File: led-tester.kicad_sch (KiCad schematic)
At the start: 19 parts, among them M1 Arduino_Mini, U1 PCF8591

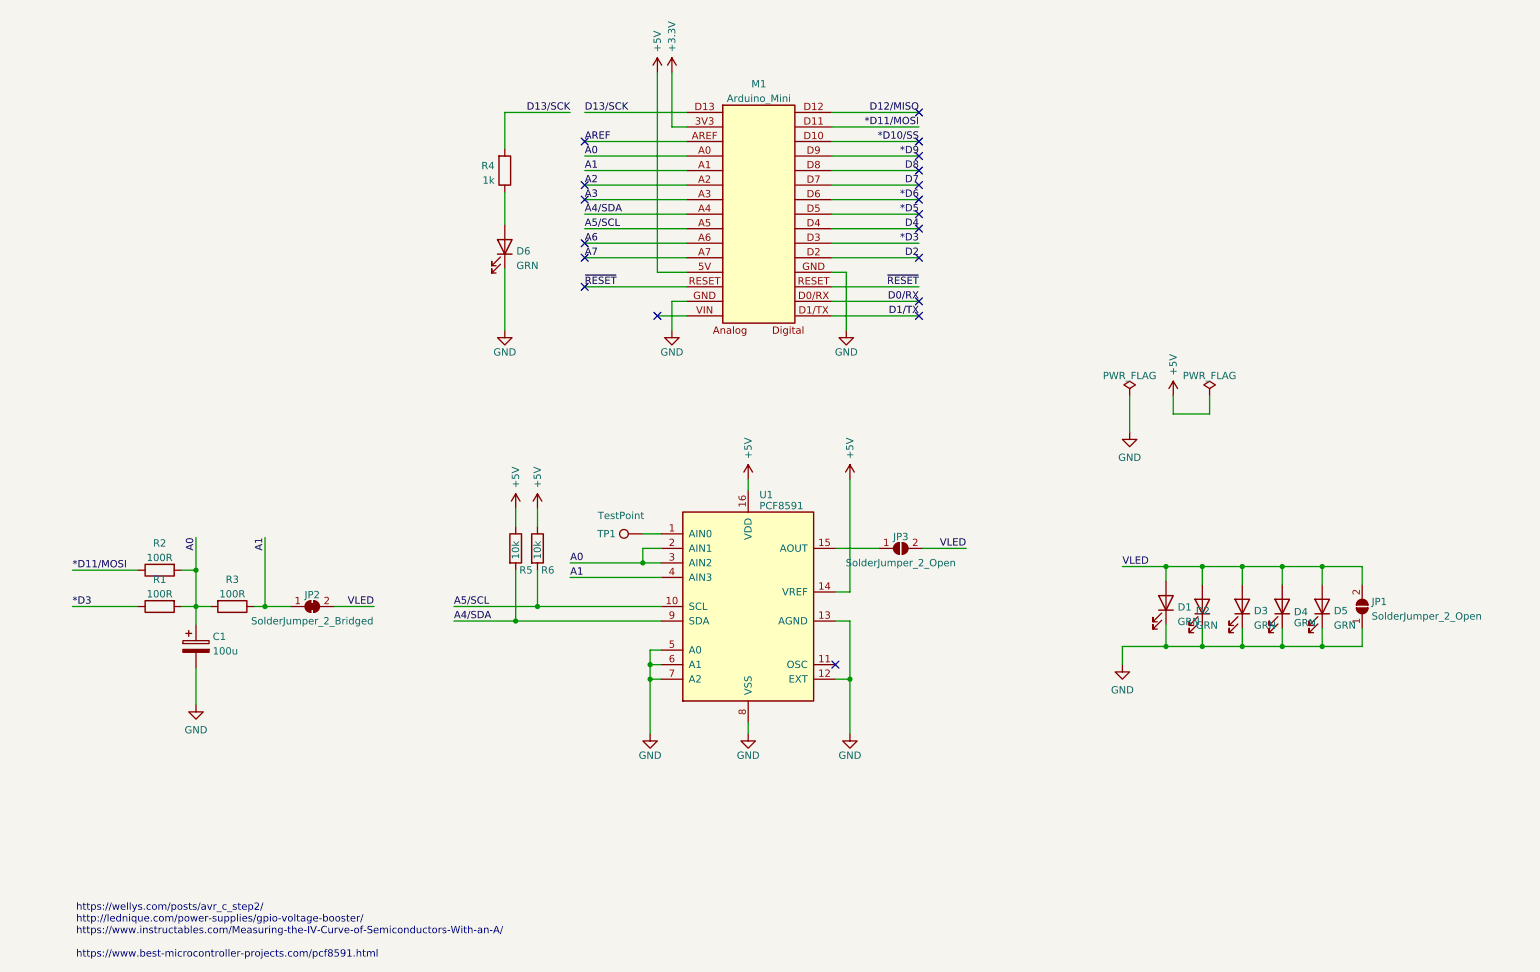
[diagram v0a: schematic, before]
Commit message: Added a current sense resistor, a decoupling cap, and rewired the PCF8591 analog inputs.
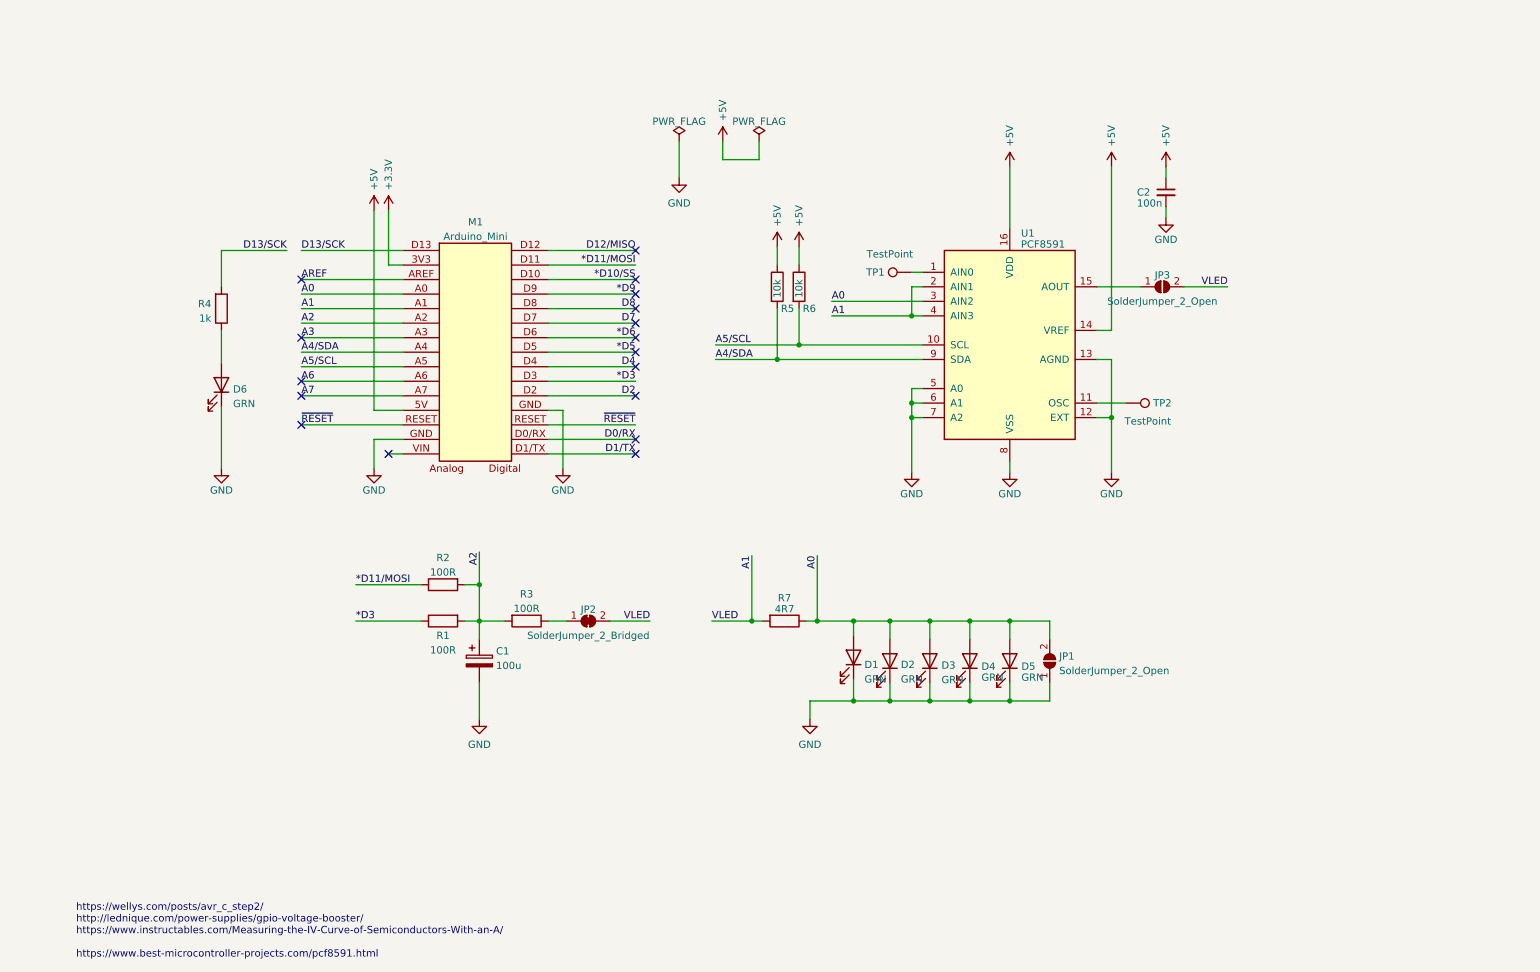
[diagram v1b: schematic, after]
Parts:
- added C2: 100n, Capacitor_SMD:C_0805_2012Metric_Pad1.18x1.45mm_HandSolder, symbol Device:C_Small
- added R7: 4R7, Resistor_SMD:R_0805_2012Metric_Pad1.20x1.40mm_HandSolder, symbol Device:R
- added TP2: TestPoint, TestPoint:TestPoint_Pad_1.5x1.5mm, symbol Connector:TestPoint
- renumbered D5 to D4, D4 to D5
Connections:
- net +5V: now also C2.1
- net A0: now also D1.2 (A), D2.2 (A), D3.2 (A), D4.2 (A), D5.2 (A), JP1.2 (B), R7.1; no longer C1.1, R1.2, R2.2, R3.2, U1.2 (AIN1)
- net A1: now also JP2.2 (B), JP3.2 (B), U1.2 (AIN1), R7.2; no longer JP2.1 (A), R3.1
- net A2: now also C1.1, R1.2, R2.2, R3.2
- net GND: now also C2.2
- net at U1.11 (OSC): now also TP2.1
- removed net VLED: D1.2 (A), D2.2 (A), D3.2 (A), D4.2 (A), D5.2 (A), JP1.2 (B), JP2.2 (B), JP3.2 (B)
- new net: JP2.1 (A), R3.1
- no-connect marks 19 -> 17
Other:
- moved on the sheet: C1, D1, D2, D3, D4, D5, D6, JP1, JP2, JP3, M1, R1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

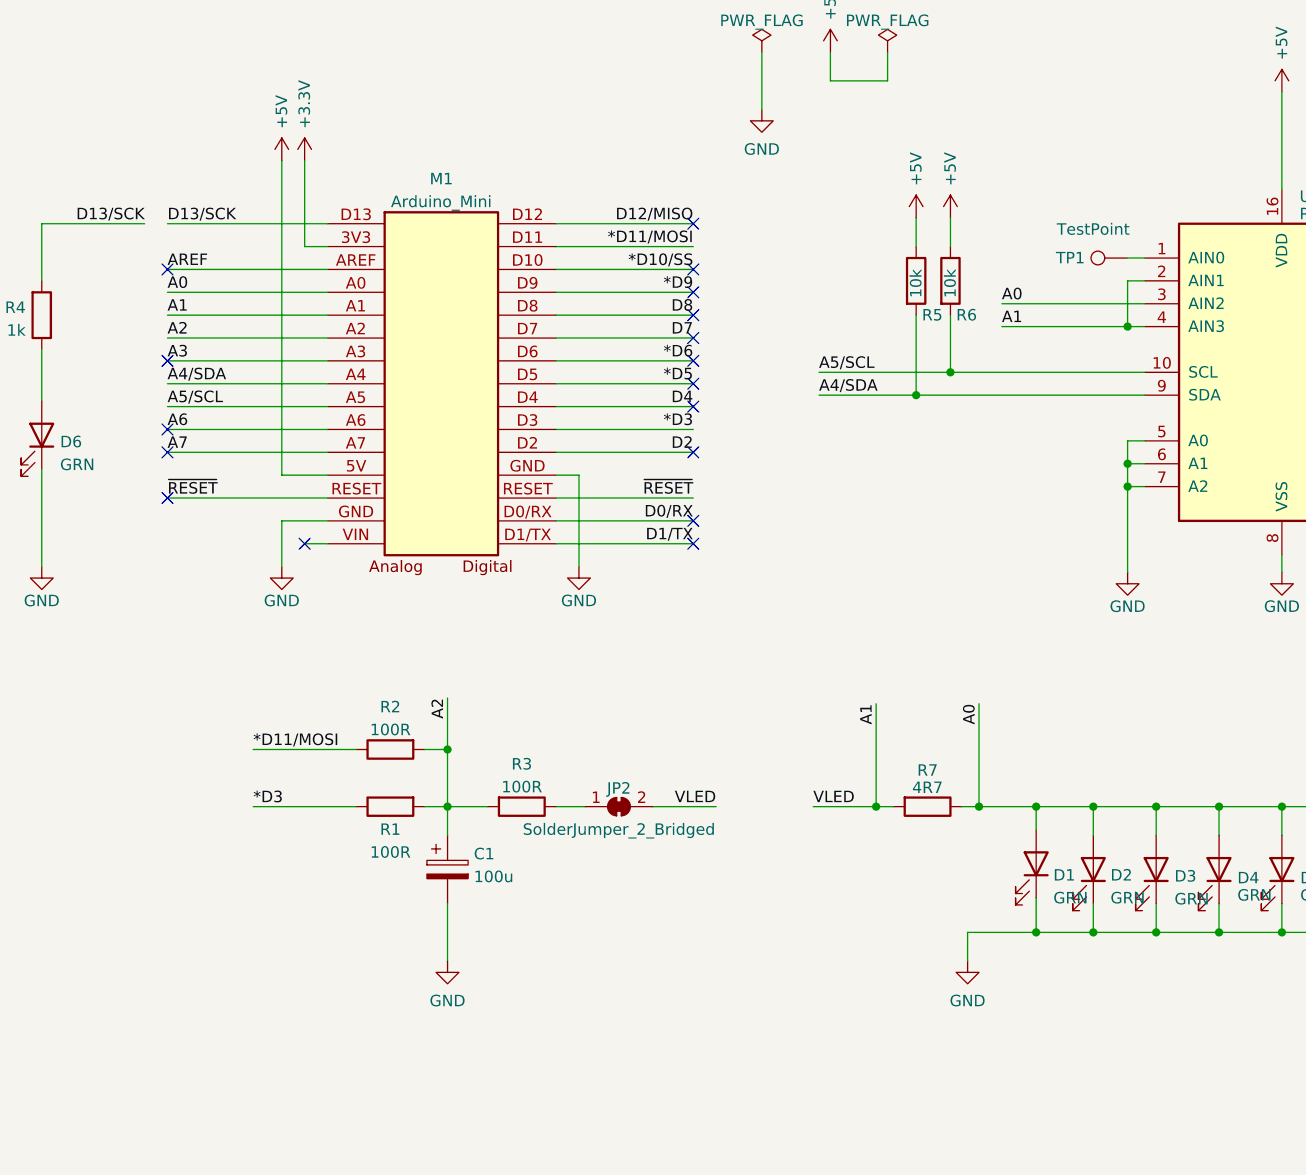
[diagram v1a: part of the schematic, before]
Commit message: Added a sense resistor between the LED under test, and GND.
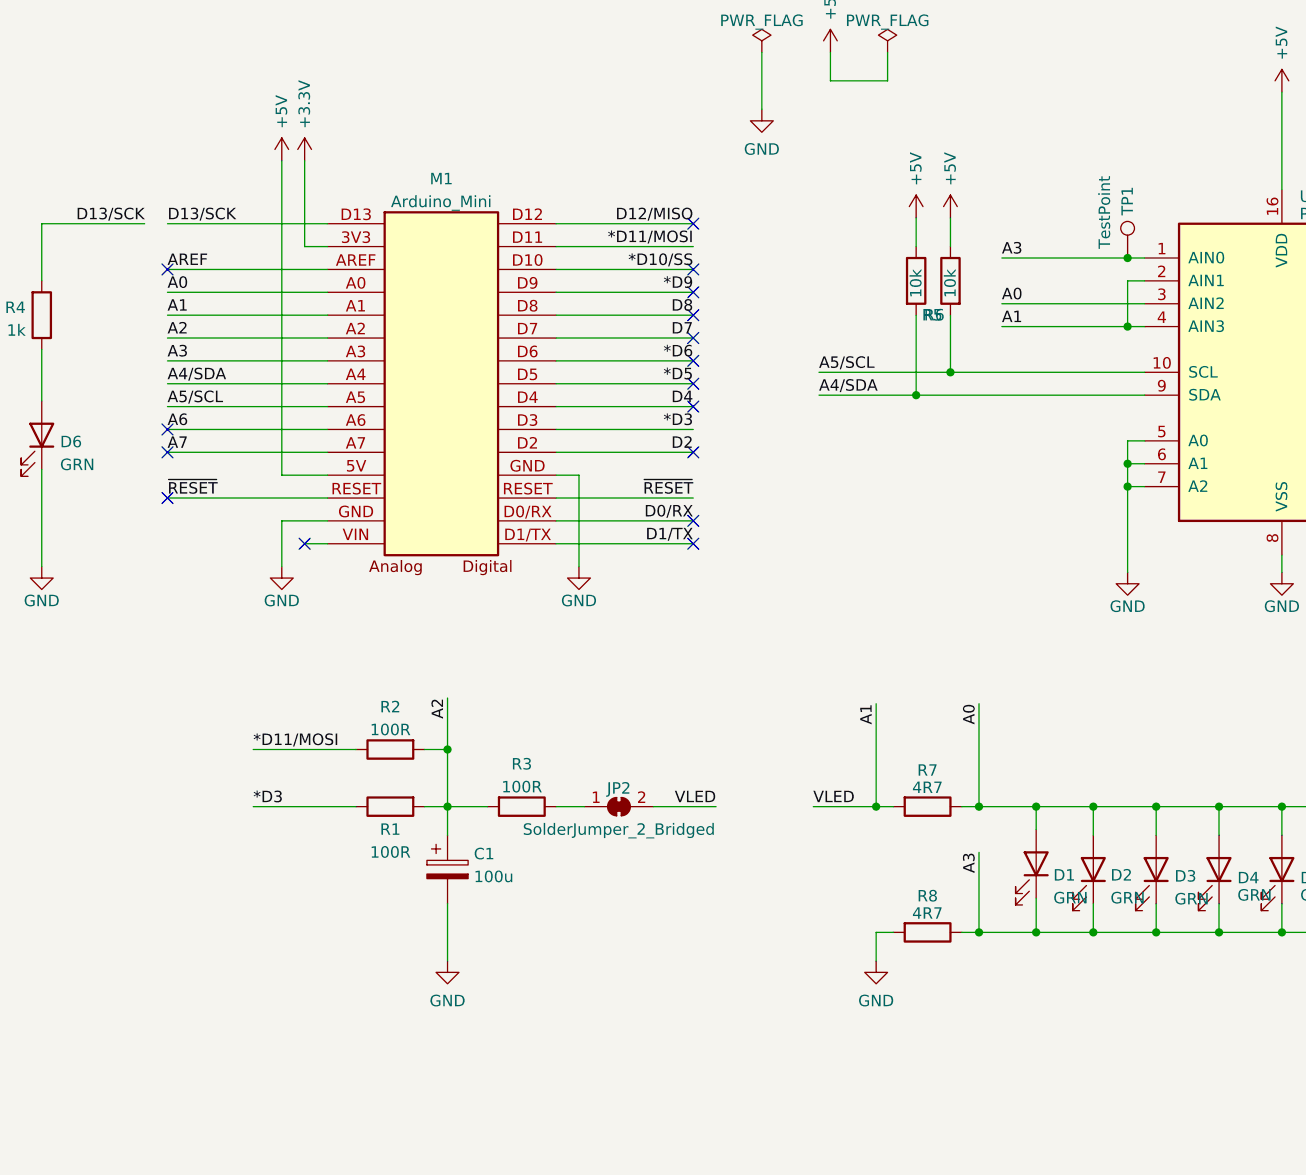
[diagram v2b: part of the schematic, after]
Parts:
- added R8: 4R7, Resistor_SMD:R_0805_2012Metric_Pad1.20x1.40mm_HandSolder, symbol Device:R
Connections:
- net A3: now also D1.1 (K), D2.1 (K), D3.1 (K), D4.1 (K), D5.1 (K), JP1.1 (A), TP1.1, U1.1 (AIN0), R8.1
- net GND: now also R8.2; no longer D1.1 (K), D2.1 (K), D3.1 (K), D4.1 (K), D5.1 (K), JP1.1 (A)
- no-connect marks 17 -> 16
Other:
- moved on the sheet: TP1
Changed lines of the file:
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@@
   (paper "A4")
   (title_block
-    (date "May 2, 2023")
-    (rev "1.0d")
+    (date "May 4, 2023")
+    (rev "1.0e")
   )
   (junction (at 154.305 83.185) (diameter 0) (color 0 0 0 0)
@@
   (junction (at 180.975 142.875) (diameter 0) (color 0 0 0 0)
   )
+  (junction (at 177.8 67.945) (diameter 0) (color 0 0 0 0)
+  )
   (junction (at 194.945 142.875) (diameter 0) (color 0 0 0 0)
   )
+  (junction (at 167.64 142.875) (diameter 0) (color 0 0 0 0)
+  )
   (junction (at 167.64 128.905) (diameter 0) (color 0 0 0 0)
   )
-  (junction (at 167.64 142.875) (diameter 0) (color 0 0 0 0)
-  )
   (junction (at 149.86 128.905) (diameter 0) (color 0 0 0 0)
+  )
+  (junction (at 161.29 142.875) (diameter 0) (color 0 0 0 0)
   )
   (junction (at 102.235 122.555) (diameter 0) (color 0 0 0 0)
@@
   (no_connect (at 129.54 64.135))
   (no_connect (at 129.54 89.535))
-  (no_connect (at 71.12 79.375))
   (no_connect (at 129.54 74.295))
   (no_connect (at 71.12 94.615))
@@
     (stroke (width 0) (type default))
   )
+  (wire (pts (xy 149.86 142.875) (xy 151.765 142.875))
+    (stroke (width 0) (type default))
+  )
   (wire (pts (xy 179.705 88.265) (xy 177.8 88.265))
     (stroke (width 0) (type default))
@@
     (stroke (width 0) (type default))
   )
+  (wire (pts (xy 161.29 133.985) (xy 161.29 142.875))
+    (stroke (width 0) (type default))
+  )
   (wire (pts (xy 161.29 117.475) (xy 161.29 128.905))
     (stroke (width 0) (type default))
@@
     (stroke (width 0) (type default))
   )
+  (wire (pts (xy 177.8 67.945) (xy 179.705 67.945))
+    (stroke (width 0) (type default))
+  )
   (wire (pts (xy 158.115 63.5) (xy 158.115 66.675))
     (stroke (width 0) (type default))
@@
     (stroke (width 0) (type default))
   )
-  (wire (pts (xy 177.8 67.945) (xy 179.705 67.945))
+  (wire (pts (xy 163.83 67.945) (xy 177.8 67.945))
     (stroke (width 0) (type default))
   )
@@
     (stroke (width 0) (type solid))
   )
-  (wire (pts (xy 167.64 142.875) (xy 160.02 142.875))
-    (stroke (width 0) (type default))
-  )
   (wire (pts (xy 161.29 128.905) (xy 167.64 128.905))
     (stroke (width 0) (type default))
@@
     (stroke (width 0) (type default))
   )
-  (wire (pts (xy 160.02 142.875) (xy 160.02 146.05))
+  (wire (pts (xy 149.86 142.875) (xy 149.86 146.05))
     (stroke (width 0) (type default))
   )
@@
     (stroke (width 0) (type default))
   )
+  (wire (pts (xy 161.29 142.875) (xy 167.64 142.875))
+    (stroke (width 0) (type default))
+  )
   (wire (pts (xy 177.8 90.805) (xy 177.8 93.345))
     (stroke (width 0) (type default))
@@
   (wire (pts (xy 71.12 86.995) (xy 88.9 86.995))
     (stroke (width 0) (type solid))
+  )
+  (wire (pts (xy 159.385 142.875) (xy 161.29 142.875))
+    (stroke (width 0) (type default))
   )
   (wire (pts (xy 201.93 128.905) (xy 201.93 132.08))
@@
     (effects (font (size 1.27 1.27)) (justify right bottom))
   )
+  (label "A3" (at 163.83 67.945 0) (fields_autoplaced)
+    (effects (font (size 1.27 1.27)) (justify left bottom))
+  )
   (label "*D5" (at 129.54 81.915 180) (fields_autoplaced)
     (effects (font (size 1.27 1.27)) (justify right bottom))
@@
   (label "A5{slash}SCL" (at 143.51 80.645 0) (fields_autoplaced)
     (effects (font (size 1.27 1.27)) (justify left bottom))
+  )
+  (label "A3" (at 161.29 133.985 270) (fields_autoplaced)
+    (effects (font (size 1.27 1.27)) (justify right bottom))
   )
   (label "A0" (at 163.83 73.025 0) (fields_autoplaced)
@@
         (path "/0d35483a-0b12-46cc-b9f2-896fd6831779"
           (reference "D5") (unit 1)
+        )
+      )
+    )
+  )
+  (symbol (lib_id "Device:R") (at 155.575 142.875 270) (unit 1)
+    (in_bom yes) (on_board yes) (dnp no) (fields_autoplaced)
+    (property "Reference" "R8" (at 155.575 138.8491 90)
+      (effects (font (size 1.27 1.27)))
+    )
+    (property "Value" "4R7" (at 155.575 140.7701 90)
+      (effects (font (size 1.27 1.27)))
+    )
+    (property "Footprint" "Resistor_SMD:R_0805_2012Metric_Pad1.20x1.40mm_HandSolder" (at 155.575 141.097 90)
+      (effects (font (size 1.27 1.27)) hide)
+    )
+    (property "Datasheet" "~" (at 155.575 142.875 0)
+      (effects (font (size 1.27 1.27)) hide)
+    )
+    (pin "1")
+    (pin "2")
+    (instances
+      (project "led-tester"
+        (path "/0d35483a-0b12-46cc-b9f2-896fd6831779"
+          (reference "R8") (unit 1)
         )
       )
@@
     )
   )
-  (symbol (lib_id "Device:R") (at 158.115 70.485 0) (unit 1)
-    (in_bom yes) (on_board yes) (dnp no)
-    (property "Reference" "R6" (at 158.75 74.295 0)
+  (symbol (lib_id "Device:R") (at 158.115 70.485 0) (mirror y) (unit 1)
+    (in_bom yes) (on_board yes) (dnp no)
+    (property "Reference" "R6" (at 157.48 74.295 0)
       (effects (font (size 1.27 1.27)) (justify left))
     )
@@
       (effects (font (size 1.27 1.27)) (justify left))
     )
-    (property "Footprint" "Resistor_SMD:R_0805_2012Metric_Pad1.20x1.40mm_HandSolder" (at 156.337 70.485 90)
+    (property "Footprint" "Resistor_SMD:R_0805_2012Metric_Pad1.20x1.40mm_HandSolder" (at 159.893 70.485 90)
       (effects (font (size 1.27 1.27)) hide)
     )
@@
     )
   )
-  (symbol (lib_id "Connector:TestPoint") (at 177.8 67.945 90) (unit 1)
-    (in_bom yes) (on_board yes) (dnp no)
-    (property "Reference" "TP1" (at 171.45 67.945 90)
-      (effects (font (size 1.27 1.27)))
-    )
-    (property "Value" "TestPoint" (at 173.99 64.77 90)
-      (effects (font (size 1.27 1.27)))
-    )
-    (property "Footprint" "TestPoint:TestPoint_THTPad_D2.0mm_Drill1.0mm" (at 177.8 62.865 0)
-      (effects (font (size 1.27 1.27)) hide)
-    )
-    (property "Datasheet" "~" (at 177.8 62.865 0)
+  (symbol (lib_id "Connector:TestPoint") (at 177.8 67.945 0) (unit 1)
+    (in_bom yes) (on_board yes) (dnp no)
+    (property "Reference" "TP1" (at 177.8 61.595 90)
+      (effects (font (size 1.27 1.27)))
+    )
+    (property "Value" "TestPoint" (at 175.26 62.865 90)
+      (effects (font (size 1.27 1.27)))
+    )
+    (property "Footprint" "TestPoint:TestPoint_THTPad_D2.0mm_Drill1.0mm" (at 182.88 67.945 0)
+      (effects (font (size 1.27 1.27)) hide)
+    )
+    (property "Datasheet" "~" (at 182.88 67.945 0)
       (effects (font (size 1.27 1.27)) hide)
     )
@@
     )
   )
-  (symbol (lib_id "power:GND") (at 160.02 146.05 0) (mirror y) (unit 1)
-    (in_bom yes) (on_board yes) (dnp no) (fields_autoplaced)
-    (property "Reference" "#PWR013" (at 160.02 152.4 0)
-      (effects (font (size 1.27 1.27)) hide)
-    )
-    (property "Value" "GND" (at 160.02 150.4934 0)
-      (effects (font (size 1.27 1.27)))
-    )
-    (property "Footprint" "" (at 160.02 146.05 0)
-      (effects (font (size 1.27 1.27)) hide)
-    )
-    (property "Datasheet" "" (at 160.02 146.05 0)
-      (effects (font (size 1.27 1.27)) hide)
-    )
+  (symbol (lib_id "power:GND") (at 149.86 146.05 0) (mirror y) (unit 1)
+    (in_bom yes) (on_board yes) (dnp no) (fields_autoplaced)
+    (property "Reference" "#PWR013" (at 149.86 152.4 0)
+      (effects (font (size 1.27 1.27)) hide)
+    )
+    (property "Value" "GND" (at 149.86 150.4934 0)
+      (effects (font (size 1.27 1.27)))
+    )
+    (property "Footprint" "" (at 149.86 146.05 0)
+      (effects (font (size 1.27 1.27)) hide)
+    )
+    (property "Datasheet" "" (at 149.86 146.05 0)
+      (effects (font (size 1.27 1.27)) hide)
+    )
